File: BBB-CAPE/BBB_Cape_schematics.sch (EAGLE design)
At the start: 71 parts, among them U10 CDCS502, U11 OPA335, U12 OPA335, U13 OPA335, U14 OPA335, U19 ADS1252, U21 REF3125, U22 OPA335, U23 ATS16ASM-1, U4 INA129, U5 TPS60403, U9 OPA335

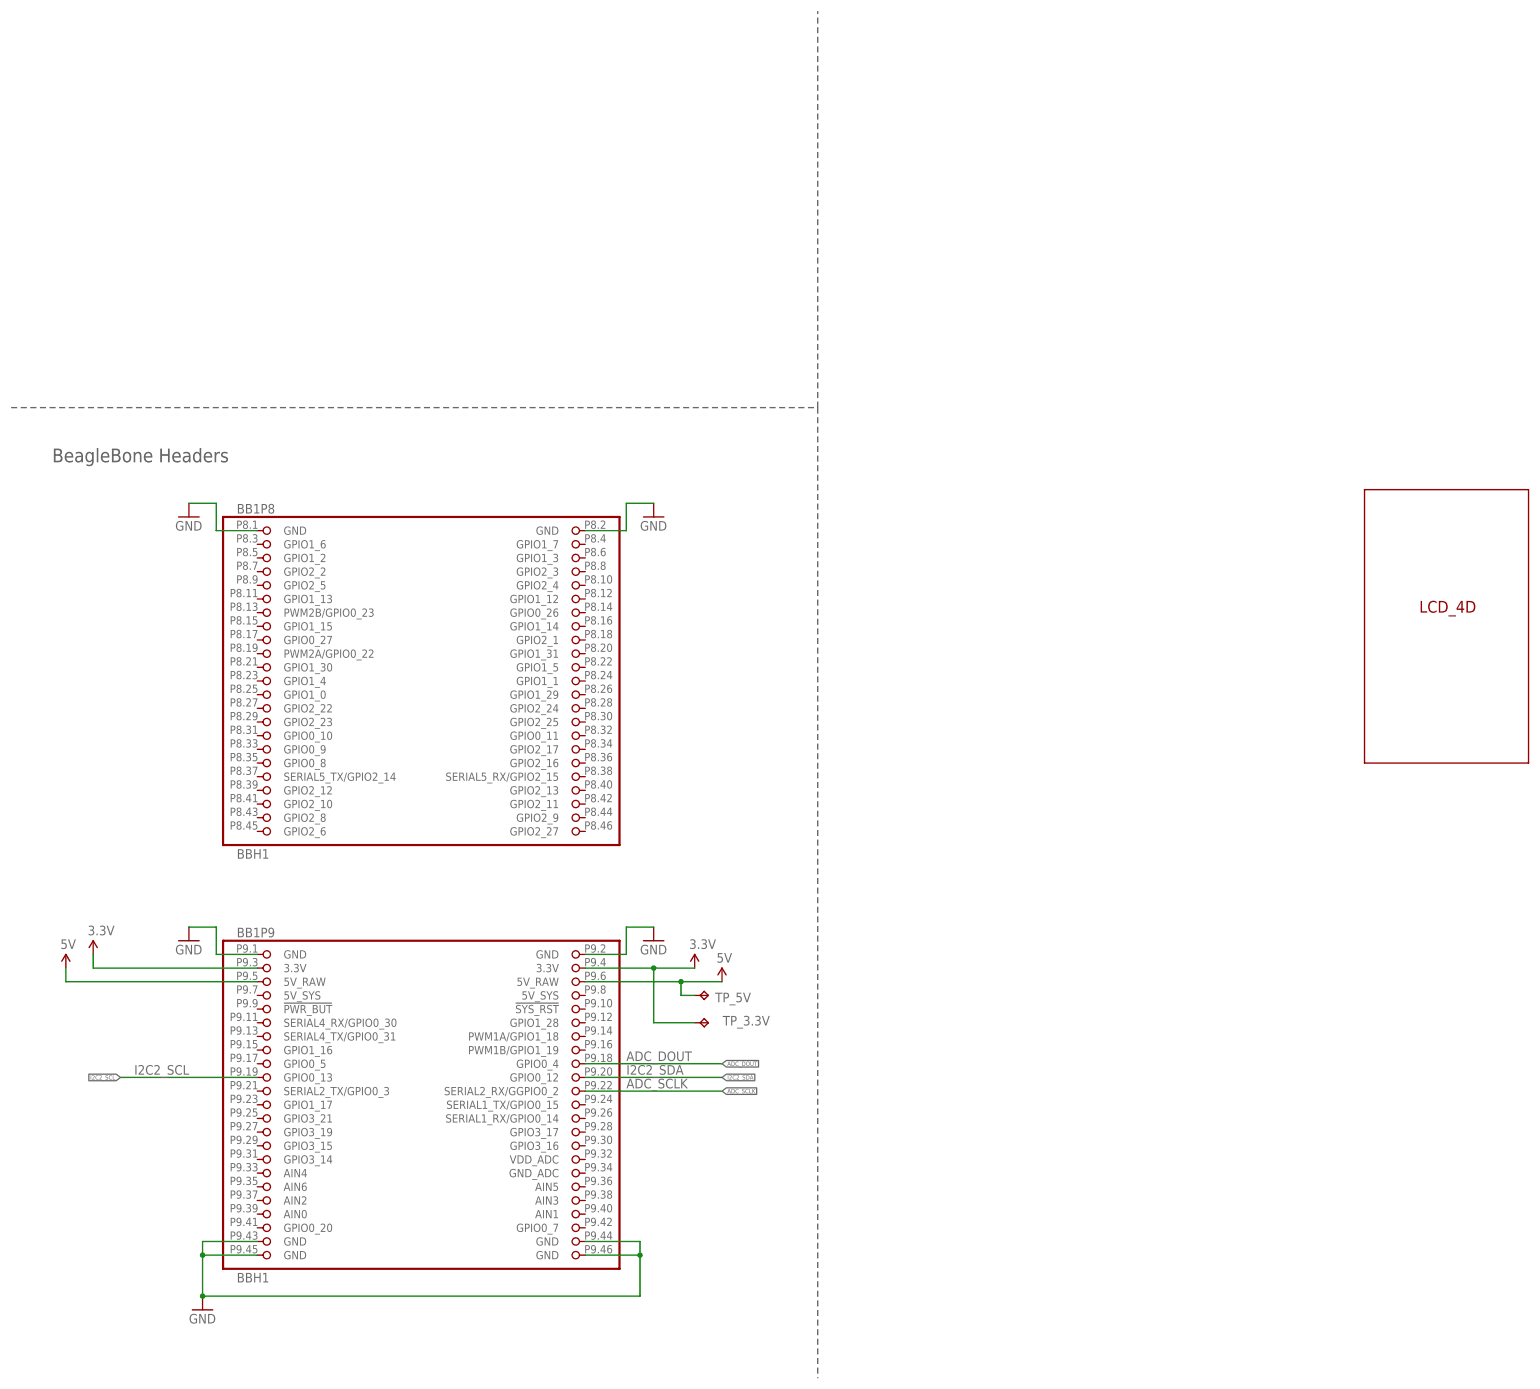
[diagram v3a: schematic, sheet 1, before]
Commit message: Modify board boundary, Change orientation of Component names in Silk screen
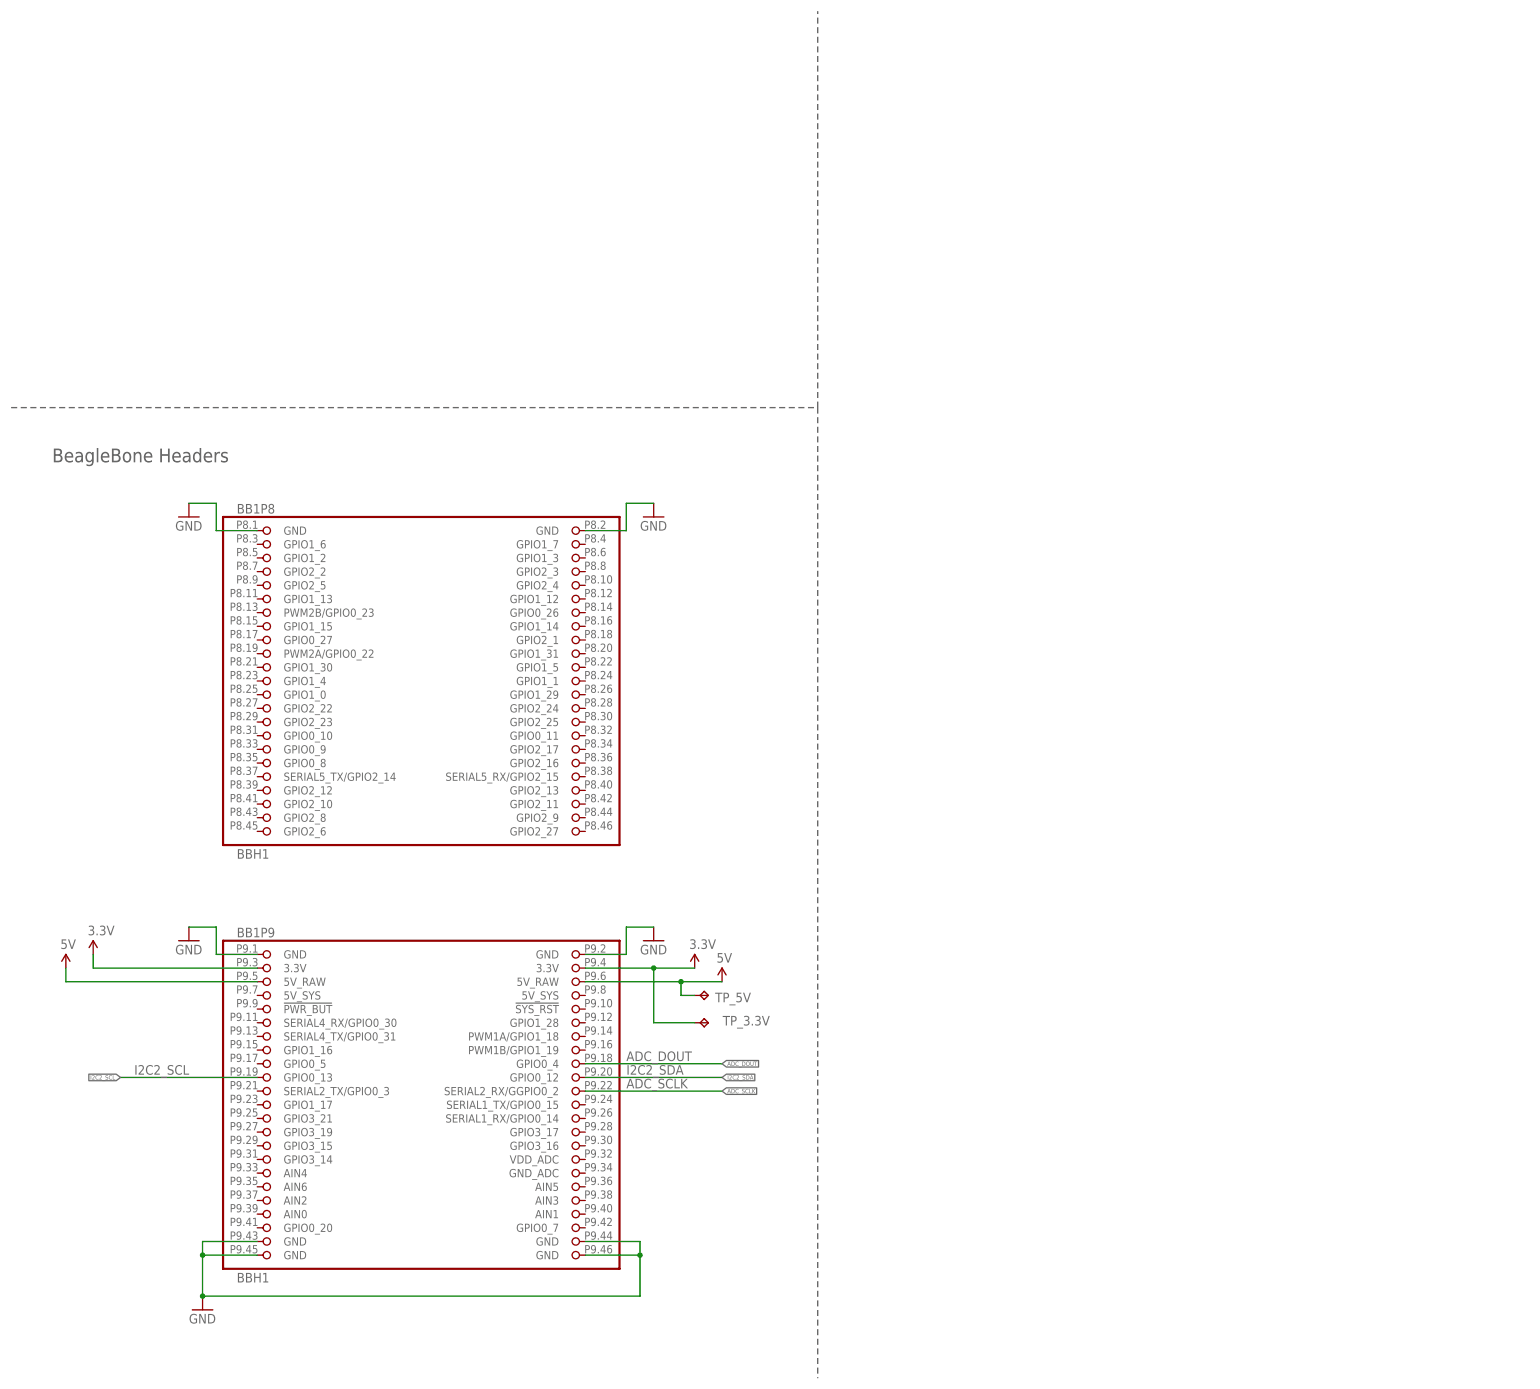
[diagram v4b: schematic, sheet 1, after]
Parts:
- removed U$25: LCD_4D, Components:LCD_4D
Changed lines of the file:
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@@
 <?xml version="1.0" encoding="utf-8"?>
 <!DOCTYPE eagle SYSTEM "eagle.dtd">
-<eagle version="6.2">
+<eagle version="6.4">
 <drawing>
 <settings>
@@
 <setting verticaltext="up"/>
 </settings>
-<grid distance="0.05" unitdist="inch" unit="inch" style="lines" multiple="1" display="yes" altdistance="0.01" altunitdist="inch" altunit="inch"/>
+<grid distance="0.1" unitdist="inch" unit="inch" style="lines" multiple="1" display="no" altdistance="0.01" altunitdist="inch" altunit="inch"/>
 <layers>
 <layer number="1" name="Top" color="4" fill="1" visible="no" active="no"/>
@@
 <part name="C12" library="rcl" deviceset="C-US" device="C1206" value="0.10uF"/>
 <part name="GND30" library="supply1" deviceset="GND" device=""/>
-<part name="U$25" library="Components" deviceset="LCD_4D" device=""/>
 <part name="C17" library="rcl" deviceset="C-US" device="C1206" value="22pF"/>
 <part name="C22" library="rcl" deviceset="C-US" device="C1206" value="22pF"/>
@@
 <instance part="U$3" gate="G$1" x="0" y="0"/>
 <instance part="U$3" gate="G$2" x="276.86" y="5.08"/>
-<instance part="BB1" gate="P8" x="78.74" y="132.08"/>
-<instance part="BB1" gate="P9" x="78.74" y="53.34"/>
+<instance part="BB1" gate="P8" x="78.74" y="132.08" smashed="yes">
+<attribute name="NAME" x="44.45" y="163.195" size="1.778" layer="95"/>
+<attribute name="VALUE" x="44.45" y="99.06" size="1.778" layer="96"/>
+</instance>
+<instance part="BB1" gate="P9" x="78.74" y="53.34" smashed="yes">
+<attribute name="NAME" x="44.45" y="84.455" size="1.778" layer="95"/>
+<attribute name="VALUE" x="44.45" y="20.32" size="1.778" layer="96"/>
+</instance>
 <instance part="TP_5V" gate="G$1" x="132.08" y="73.66" smashed="yes" rot="R270">
 <attribute name="NAME" x="133.35" y="72.39" size="1.778" layer="95"/>
@@
 <attribute name="TP_SIGNAL_NAME" x="130.81" y="67.31" size="1.778" layer="97" rot="R270"/>
 </instance>
-<instance part="U$25" gate="G$1" x="269.24" y="142.24"/>
 </instances>
 <busses>

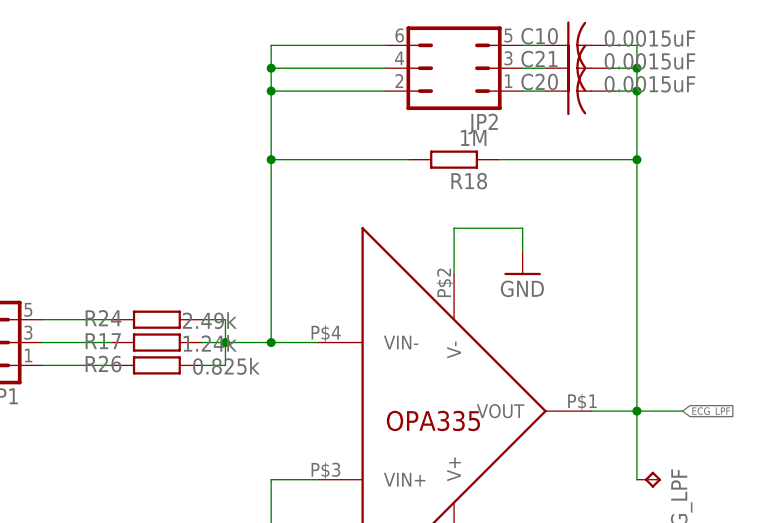
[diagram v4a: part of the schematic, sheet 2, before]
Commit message: Update Resistor and Capacitor value in BBB_Cape_schematics.sch
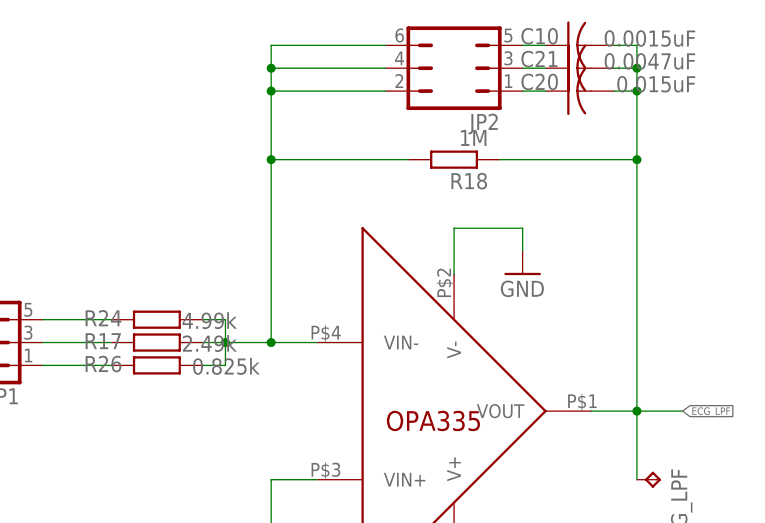
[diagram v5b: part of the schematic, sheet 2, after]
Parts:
- C20: value 0.0015uF -> 0.015uF
- C21: value 0.0015uF -> 0.0047uF
- R17: value 1.24k -> 2.49k
- R19: value 100k -> 10k
- R24: value 2.49k -> 4.99k
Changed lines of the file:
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@@
 <?xml version="1.0" encoding="utf-8"?>
 <!DOCTYPE eagle SYSTEM "eagle.dtd">
-<eagle version="6.4">
+<eagle version="6.2">
 <drawing>
 <settings>
@@
 <setting verticaltext="up"/>
 </settings>
-<grid distance="0.1" unitdist="inch" unit="inch" style="lines" multiple="1" display="no" altdistance="0.01" altunitdist="inch" altunit="inch"/>
+<grid distance="0.1" unitdist="inch" unit="inch" style="lines" multiple="1" display="yes" altdistance="0.01" altunitdist="inch" altunit="inch"/>
 <layers>
 <layer number="1" name="Top" color="4" fill="1" visible="no" active="no"/>
@@
 <part name="SUPPLY5" library="supply2" deviceset="+5V/2" device=""/>
 <part name="U13" library="Components" deviceset="OPA335" device=""/>
-<part name="R17" library="resistor" deviceset="R-EU_" device="M1206" value="1.24k"/>
+<part name="R17" library="resistor" deviceset="R-EU_" device="M1206" value="2.49k"/>
 <part name="R18" library="resistor" deviceset="R-EU_" device="M1206" value="1M"/>
 <part name="SUPPLY6" library="supply2" deviceset="+5V/2" device=""/>
@@
 <part name="C13" library="rcl" deviceset="C-US" device="C1206" value="0.1uF"/>
 <part name="GND22" library="supply1" deviceset="GND" device=""/>
-<part name="R19" library="resistor" deviceset="R-EU_" device="M1206" value="100k"/>
+<part name="R19" library="resistor" deviceset="R-EU_" device="M1206" value="10k"/>
 <part name="C14" library="rcl" deviceset="C-US" device="C1206" value="0.1uF"/>
 <part name="C15" library="rcl" deviceset="C-US" device="C1206" value="10uF"/>
@@
 <part name="R23" library="resistor" deviceset="R-EU_" device="M1206" value="80.6k"/>
 <part name="GND27" library="supply1" deviceset="GND" device=""/>
-<part name="R24" library="resistor" deviceset="R-EU_" device="M1206" value="2.49k"/>
+<part name="R24" library="resistor" deviceset="R-EU_" device="M1206" value="4.99k"/>
 <part name="R26" library="resistor" deviceset="R-EU_" device="M1206" value="0.825k"/>
 <part name="C10" library="rcl" deviceset="C-US" device="C1206" value="0.0015uF"/>
-<part name="C20" library="rcl" deviceset="C-US" device="C1206" value="0.0015uF"/>
-<part name="C21" library="rcl" deviceset="C-US" device="C1206" value="0.0015uF"/>
+<part name="C20" library="rcl" deviceset="C-US" device="C1206" value="0.015uF"/>
+<part name="C21" library="rcl" deviceset="C-US" device="C1206" value="0.0047uF"/>
 <part name="RH_INDEX" library="Components" deviceset="PAD" device=""/>
 <part name="GND28" library="supply1" deviceset="GND" device=""/>
